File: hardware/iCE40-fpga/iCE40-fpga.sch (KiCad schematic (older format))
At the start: 47 parts, among them J1 USB_B_Micro, J2 JST_PH, J3 Feather, Q1 DMP2045U, U1 MCP73831-2-OT, U2 W25Q32JVZP, U3 AP2112K-3.3, U4 ICE40UP5K-SG48ITR, U5 AP2112K-1.2, X1 DSC6101CI1A

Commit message: fixing things which broke resulting from library change
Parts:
- removed J3: Feather, josh-connectors:featherwing, symbol josh-mechnanical:Feather
- added J3: Feather, josh-connectors:featherwing, symbol josh-connector:Feather
- U4: footprint josh-dfn-qfn:QFN-48-1EP_7x7mm_P0.5mm_EP5.3x5.3mm_ThermalVias -> josh-dfn-qfn:QFN-48-1EP_7x7mm_P0.5mm_EP5.6x5.6mm_ThermalVias
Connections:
- net +3V3: now also J3.2 (3V3)
- net +5V: now also J3.26 (VBUS)
- net +BATT: now also J3.28 (VBAT)
- net GND: now also J3.16 (NC), J3.4 (GND)
- net IO0: now also J3.5 (IO0)
- net IO1: now also J3.6 (IO1)
- net IO10: now also J3.15 (IO10|TX)
- net IO11: now also J3.17 (IO11|SDA)
- net IO12: now also J3.18 (IO12|SCL)
- net IO13: now also J3.19 (IO13)
- net IO14: now also J3.20 (IO14)
- net IO15: now also J3.21 (IO15)
- net IO16: now also J3.22 (IO16)
- net IO17: now also J3.23 (IO17)
- net IO18: now also J3.24 (IO18)
- net IO19: now also J3.25 (IO19)
- net IO2: now also J3.7 (IO2)
- net IO3: now also J3.8 (IO3)
- net IO4: now also J3.9 (IO4)
- net IO5: now also J3.10 (IO5)
- net IO6: now also J3.11 (IO6|SCK)
- net IO7: now also J3.12 (IO7|MOSI)
- net IO8: now also J3.13 (IO8|MISO)
- net IO9: now also J3.14 (IO9|RX)
- net LDO_EN: now also J3.27 (EN)
- net nICE_CRESET: now also J3.1 (nRST)
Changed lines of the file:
@@
 Text Notes 3800 4425 0    118  ~ 0
 SPI Flash
-$Comp
-L Device:C C7
-U 1 1 5E13AD65
-P 4475 5175
-F 0 "C7" H 4500 5275 50  0000 L CNN
-F 1 "100n" H 4500 5075 50  0000 L CNN
-F 2 "Capacitor_SMD:C_0603_1608Metric" H 4513 5025 50  0001 C CNN
-F 3 "~" H 4475 5175 50  0001 C CNN
-	1    4475 5175
-	1    0    0    -1
-$EndComp
-Wire Wire Line
-	4400 4975 4475 4975
-Wire Wire Line
-	4475 4975 4475 5025
-Wire Wire Line
-	4475 5325 4475 5375
-Wire Wire Line
-	4475 4975 4475 4950
-Connection ~ 4475 4975
-$Comp
-L power:+3V3 #PWR031
-U 1 1 5E189B67
-P 4475 4950
-F 0 "#PWR031" H 4475 4800 50  0001 C CNN
-F 1 "+3V3" H 4490 5123 50  0000 C CNN
-F 2 "" H 4475 4950 50  0001 C CNN
-F 3 "" H 4475 4950 50  0001 C CNN
-	1    4475 4950
-	1    0    0    -1
-$EndComp
-$Comp
-L power:GND #PWR032
-U 1 1 5E18A045
-P 4475 5500
-F 0 "#PWR032" H 4475 5250 50  0001 C CNN
-F 1 "GND" H 4480 5327 50  0000 C CNN
-F 2 "" H 4475 5500 50  0001 C CNN
-F 3 "" H 4475 5500 50  0001 C CNN
-	1    4475 5500
-	1    0    0    -1
-$EndComp
 Text Label 2575 5075 0    50   ~ 0
 ICE_SCK
@@
 Text Label 2575 5275 0    50   ~ 0
 FLASH_MISO|IO1
-Wire Wire Line
-	2575 5175 3700 5175
 Wire Wire Line
 	3425 4525 3425 4475
@@
 $EndComp
 Wire Wire Line
-	4400 5375 4475 5375
-Connection ~ 4475 5375
-Wire Wire Line
-	4400 5475 4475 5475
-Connection ~ 4475 5475
-Wire Wire Line
-	4475 5475 4475 5500
-Wire Wire Line
-	4475 5375 4475 5475
-Wire Wire Line
 	10925 1975 10875 1975
 Wire Wire Line
@@
 Connection ~ 3525 4975
 Wire Wire Line
-	3525 4975 3700 4975
-Wire Wire Line
-	2575 5275 3700 5275
-Wire Wire Line
 	2575 4975 3525 4975
 Wire Wire Line
@@
 	3225 4925 3225 5075
 Connection ~ 3225 5075
-Wire Wire Line
-	3225 5075 3700 5075
 Wire Wire Line
 	6425 1300 6900 1300
@@
 Connection ~ 3325 5375
 Wire Wire Line
-	3325 5375 3700 5375
-Wire Wire Line
 	3425 4925 3425 5475
 Connection ~ 3425 5475
-Wire Wire Line
-	3425 5475 3700 5475
 $Comp
 L josh-ic:ICE40UP5K-SG48ITR U4
@@
 F 0 "U4" H 7000 2700 50  0000 L CNN
 F 1 "ICE40UP5K-SG48ITR" V 7550 1400 50  0000 L CNN
-F 2 "josh-dfn-qfn:QFN-48-1EP_7x7mm_P0.5mm_EP5.3x5.3mm_ThermalVias" H 7300 450 50  0001 C CNN
+F 2 "josh-dfn-qfn:QFN-48-1EP_7x7mm_P0.5mm_EP5.6x5.6mm_ThermalVias" H 7300 450 50  0001 C CNN
 F 3 "http://www.latticesemi.com/Products/FPGAandCPLD/iCE40Ultra" H 6900 2800 50  0001 C CNN
 	1    7300 1800
@@
 F 0 "U4" H 7700 2800 50  0000 C CNN
 F 1 "ICE40UP5K-SG48ITR" V 8325 1900 50  0000 C CNN
-F 2 "josh-dfn-qfn:QFN-48-1EP_7x7mm_P0.5mm_EP5.3x5.3mm_ThermalVias" H 8025 500 50  0001 C CNN
+F 2 "josh-dfn-qfn:QFN-48-1EP_7x7mm_P0.5mm_EP5.6x5.6mm_ThermalVias" H 8025 500 50  0001 C CNN
 F 3 "http://www.latticesemi.com/Products/FPGAandCPLD/iCE40Ultra" H 7625 2850 50  0001 C CNN
 	2    8025 1850
@@
 F 0 "U4" V 8517 5075 50  0000 C CNN
 F 1 "ICE40UP5K-SG48ITR" V 8426 5075 50  0000 C CNN
-F 2 "josh-dfn-qfn:QFN-48-1EP_7x7mm_P0.5mm_EP5.3x5.3mm_ThermalVias" H 8150 3725 50  0001 C CNN
+F 2 "josh-dfn-qfn:QFN-48-1EP_7x7mm_P0.5mm_EP5.6x5.6mm_ThermalVias" H 8150 3725 50  0001 C CNN
 F 3 "http://www.latticesemi.com/Products/FPGAandCPLD/iCE40Ultra" H 7750 6075 50  0001 C CNN
 	4    8150 5075
@@
 F 0 "U4" H 7000 3975 50  0000 L CNN
 F 1 "ICE40UP5K-SG48ITR" V 7550 3075 50  0000 L CNN
-F 2 "josh-dfn-qfn:QFN-48-1EP_7x7mm_P0.5mm_EP5.3x5.3mm_ThermalVias" H 7300 2125 50  0001 C CNN
+F 2 "josh-dfn-qfn:QFN-48-1EP_7x7mm_P0.5mm_EP5.6x5.6mm_ThermalVias" H 7300 2125 50  0001 C CNN
 F 3 "http://www.latticesemi.com/Products/FPGAandCPLD/iCE40Ultra" H 6900 4475 50  0001 C CNN
 	3    7300 3475
@@
 $EndComp
 $Comp
-L josh-mechnanical:Feather J3
-U 1 1 5D18E7FC
-P 10075 4200
-F 0 "J3" H 10100 5165 50  0000 C CNN
-F 1 "Feather" H 10100 5074 50  0000 C CNN
-F 2 "josh-connectors:featherwing" H 10275 3250 50  0001 C CNN
-F 3 "" H 10275 3250 50  0001 C CNN
-	1    10075 4200
-	1    0    0    -1
-$EndComp
-$Comp
 L josh-power:MCP73831-2-OT U1
 U 1 1 5D1900C1
@@
 F 3 "http://ww1.microchip.com/downloads/en/DeviceDoc/20001984g.pdf" H 1250 5000 50  0001 C CNN
 	1    1400 5050
-	1    0    0    -1
-$EndComp
-$Comp
-L josh-memory:W25Q32JVZP U2
-U 1 1 5D1A5CE7
-P 4200 5175
-F 0 "U2" H 4050 5642 50  0000 C CNN
-F 1 "W25Q32JVZP" H 4050 5551 50  0000 C CNN
-F 2 "josh-soic-sot-etc:WSON-8-1EP_6x5mm_P1.27mm_EP3.4x4.3mm" H 4200 5175 50  0001 C CNN
-F 3 "http://www.winbond.com/resource-files/w25q32jv%20revg%2003272018%20plus.pdf" H 4200 5175 50  0001 C CNN
-	1    4200 5175
 	1    0    0    -1
 $EndComp
@@
 	1    0    0    -1
 $EndComp
+Wire Wire Line
+	3425 5475 3700 5475
+Wire Wire Line
+	3225 5075 3700 5075
+Wire Wire Line
+	2575 5175 3700 5175
+Wire Wire Line
+	3325 5375 3700 5375
+Wire Wire Line
+	2575 5275 3700 5275
+Wire Wire Line
+	3525 4975 3700 4975
+Wire Wire Line
+	4475 5375 4475 5475
+Wire Wire Line
+	4475 5475 4475 5500
+Connection ~ 4475 5475
+Wire Wire Line
+	4400 5475 4475 5475
+Connection ~ 4475 5375
+Wire Wire Line
+	4400 5375 4475 5375
+$Comp
+L power:GND #PWR032
+U 1 1 5E18A045
+P 4475 5500
+F 0 "#PWR032" H 4475 5250 50  0001 C CNN
+F 1 "GND" H 4480 5327 50  0000 C CNN
+F 2 "" H 4475 5500 50  0001 C CNN
+F 3 "" H 4475 5500 50  0001 C CNN
+	1    4475 5500
+	1    0    0    -1
+$EndComp
+$Comp
+L power:+3V3 #PWR031
+U 1 1 5E189B67
+P 4475 4950
+F 0 "#PWR031" H 4475 4800 50  0001 C CNN
+F 1 "+3V3" H 4490 5123 50  0000 C CNN
+F 2 "" H 4475 4950 50  0001 C CNN
+F 3 "" H 4475 4950 50  0001 C CNN
+	1    4475 4950
+	1    0    0    -1
+$EndComp
+Connection ~ 4475 4975
+Wire Wire Line
+	4475 4975 4475 4950
+Wire Wire Line
+	4475 5325 4475 5375
+Wire Wire Line
+	4475 4975 4475 5025
+Wire Wire Line
+	4400 4975 4475 4975
+$Comp
+L Device:C C7
+U 1 1 5E13AD65
+P 4475 5175
+F 0 "C7" H 4500 5275 50  0000 L CNN
+F 1 "100n" H 4500 5075 50  0000 L CNN
+F 2 "Capacitor_SMD:C_0603_1608Metric" H 4513 5025 50  0001 C CNN
+F 3 "~" H 4475 5175 50  0001 C CNN
+	1    4475 5175
+	1    0    0    -1
+$EndComp
+$Comp
+L josh-memory:W25Q32JVZP U2
+U 1 1 5D1A5CE7
+P 4200 5175
+F 0 "U2" H 4050 5642 50  0000 C CNN
+F 1 "W25Q32JVZP" H 4050 5551 50  0000 C CNN
+F 2 "josh-soic-sot-etc:WSON-8-1EP_6x5mm_P1.27mm_EP3.4x4.3mm" H 4200 5175 50  0001 C CNN
+F 3 "http://www.winbond.com/resource-files/w25q32jv%20revg%2003272018%20plus.pdf" H 4200 5175 50  0001 C CNN
+	1    4200 5175
+	1    0    0    -1
+$EndComp
+$Comp
+L josh-connector:Feather J3
+U 1 1 5D167739
+P 10075 4200
+F 0 "J3" H 10100 5165 50  0000 C CNN
+F 1 "Feather" H 10100 5074 50  0000 C CNN
+F 2 "josh-connectors:featherwing" H 10275 3250 50  0001 C CNN
+F 3 "" H 10275 3250 50  0001 C CNN
+	1    10075 4200
+	1    0    0    -1
+$EndComp

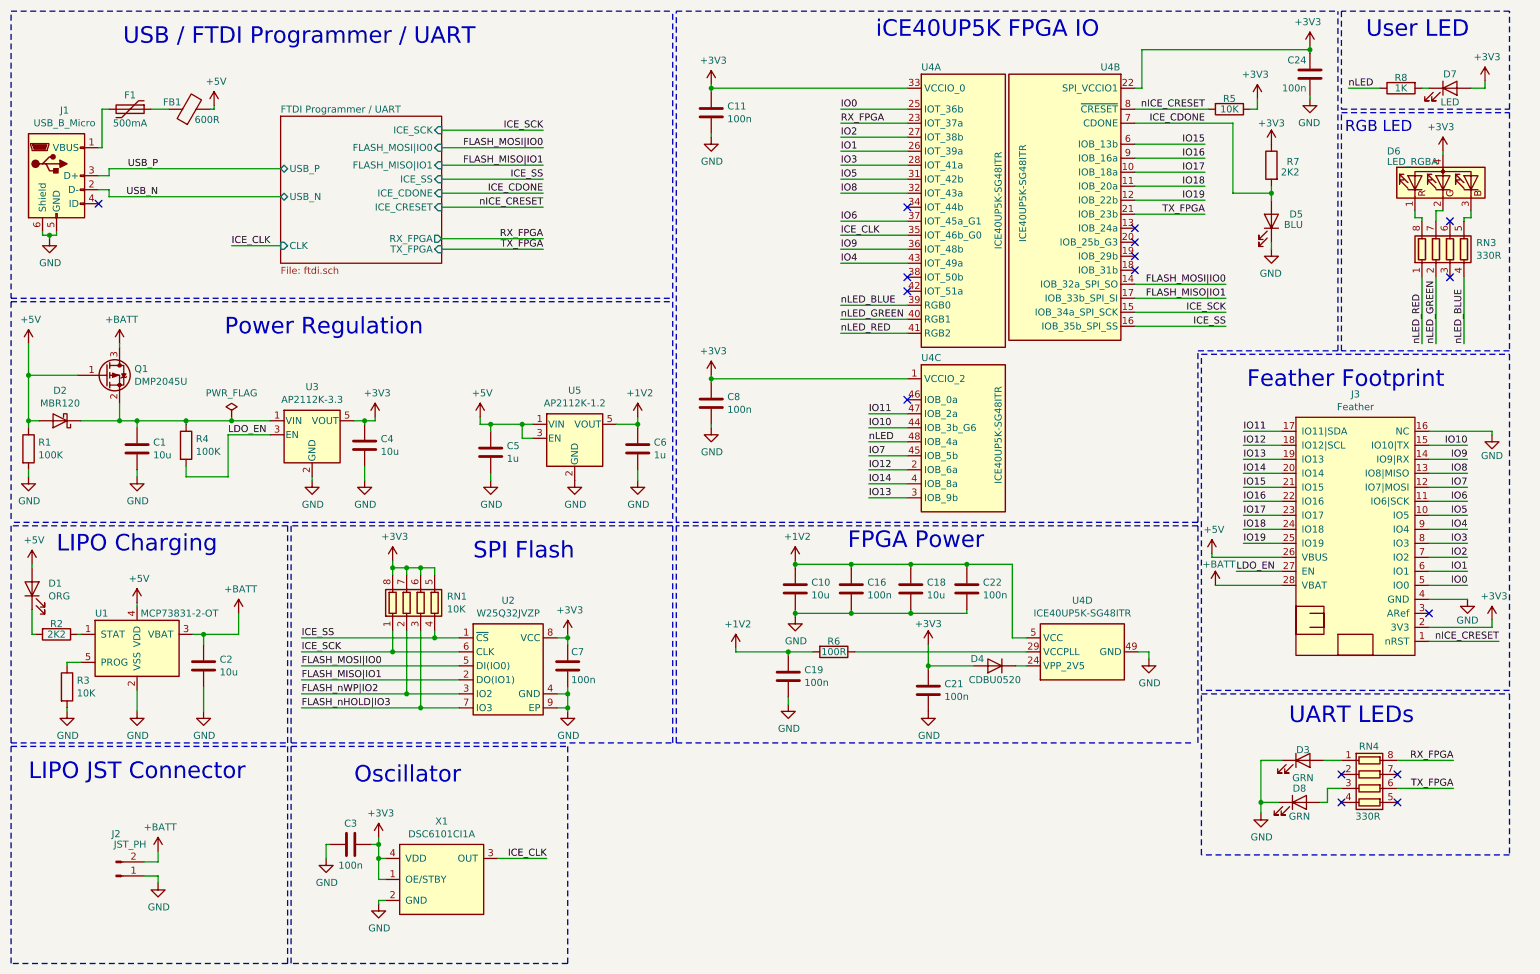
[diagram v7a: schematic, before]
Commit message: added multiplexing featherwing
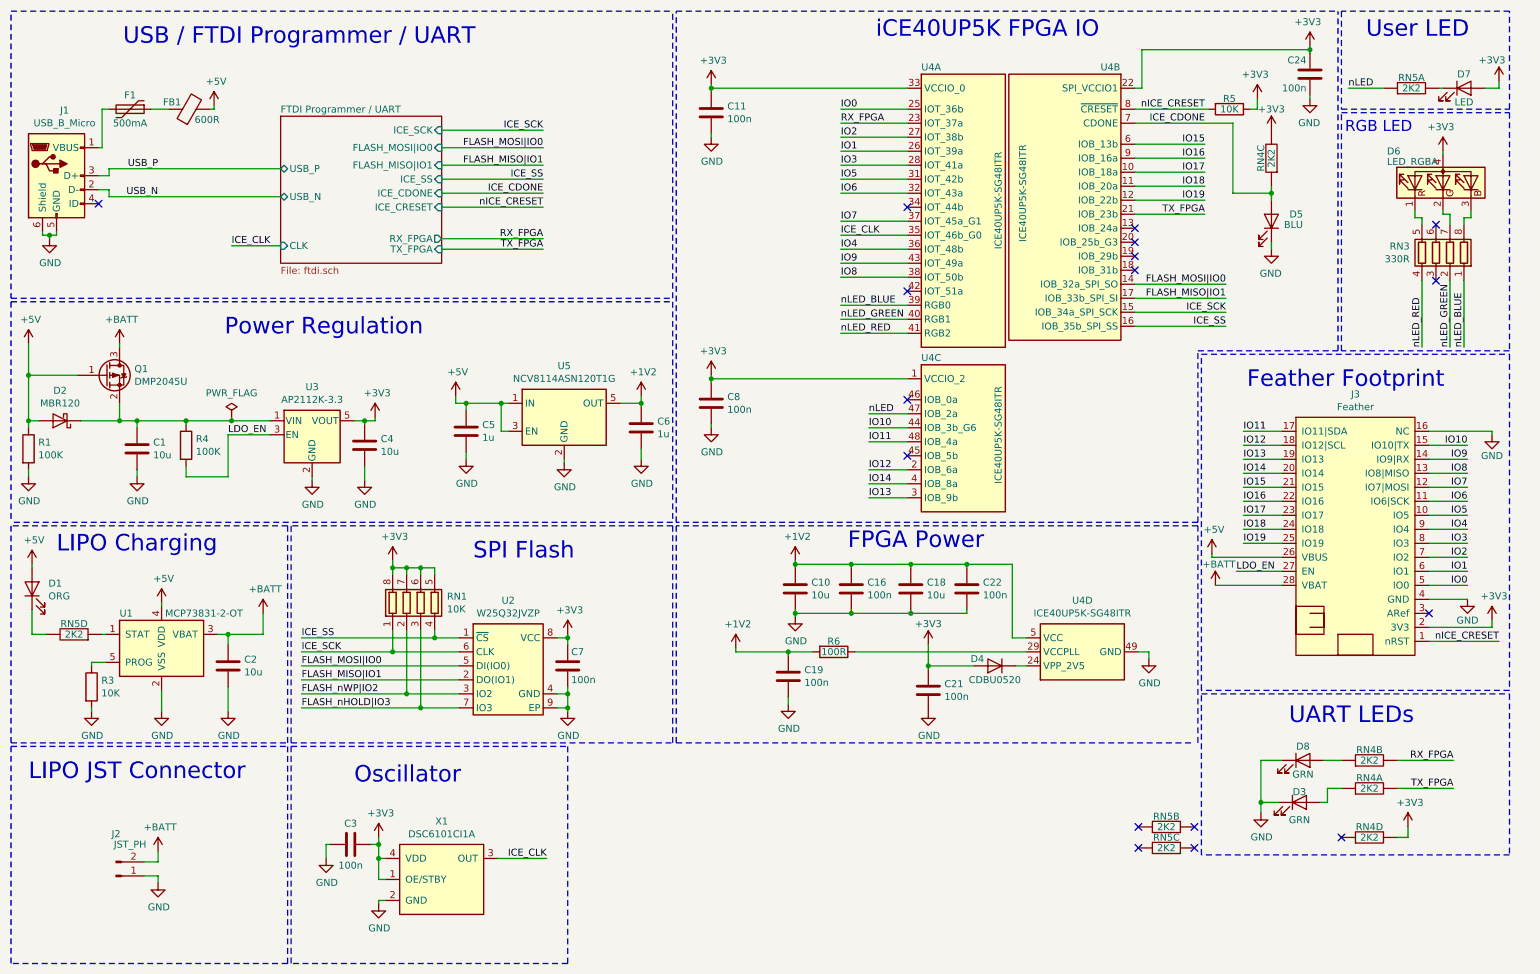
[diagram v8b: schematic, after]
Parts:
- removed R2, R7: 2K2, Resistor_SMD:R_0603_1608Metric, symbol Device:R
- removed R8: 1K, Resistor_SMD:R_0603_1608Metric, symbol Device:R
- removed RN4: 330R, Resistor_SMD:R_Array_Convex_4x0402, symbol Device:R_Pack04
- removed U5: AP2112K-1.2, Package_TO_SOT_SMD:SOT-23-5, symbol Regulator_Linear:AP2112K-1.2
- added RN4, RN5: 2K2, Resistor_SMD:R_Array_Convex_4x0402, symbol josh-passive:RN
- added U5: NCV8114ASN120T1G, Package_TO_SOT_SMD:TSOT-23-5, symbol Regulator_Linear:NCV8114ASN120T1G
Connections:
- net +1V2: now also U5.5 (OUT)
- net +3V3: now also RN4.7, RN4.8
- net +5V: now also U5.1 (IN), U5.3 (EN)
- net GND: now also U5.2 (GND)
- net ICE_CDONE: now also RN4.2
- net IO11: now also U4.48 (IOB_4a); no longer U4.47 (IOB_2a)
- net IO4: now also U4.36 (IOT_48b); no longer U4.43 (IOT_49a)
- net IO6: now also U4.32 (IOT_43a); no longer U4.37 (IOT_45a_G1)
- net IO7: now also U4.37 (IOT_45a_G1); no longer U4.45 (IOB_5b)
- net IO8: now also U4.38 (IOT_50b); no longer U4.32 (IOT_43a)
- net IO9: now also U4.43 (IOT_49a); no longer U4.36 (IOT_48b)
- net RX_FPGA: now also RN4.6
- net TX_FPGA: now also RN4.5
- net nLED: now also U4.47 (IOB_2a), RN5.4; no longer U4.48 (IOB_4a)
- net nLED_BLUE: now also RN3.1 (R1.1); no longer RN3.4 (R4.1)
- net nLED_RED: now also RN3.4 (R4.1); no longer RN3.1 (R1.1)
- net at D8.2 (A): now also RN4.3
- net at D3.2 (A): now also RN4.4
- net at D6.1 (RK): now also RN3.5 (R4.2); no longer RN3.8 (R1.2)
- net at D6.3 (BK): now also RN3.8 (R1.2); no longer RN3.5 (R4.2)
- net at U1.1 (STAT): now also RN5.1
- net at D7.1 (K): now also RN5.5
- net at D1.1 (K): now also RN5.8
- no-connect marks 16 -> 17
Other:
- moved on the sheet: C2, C5, C6, D3, D7, D8, R3, RN3, U1
